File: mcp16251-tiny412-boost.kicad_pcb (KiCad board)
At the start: 2 copper layers, 33 x 22.9 mm, 33 parts, among them J1 THT_Castellated, J2 JST_PH_Header, J3 THT_Castellated, J4 THT_Castellated, J5 THT_Castellated, J6 THT_Castellated, Q1 Q_PMOS_GSD, Q2 NPN_3904, Q3 Q_PMOS_GSD, Q4 Q_PMOS_GSD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

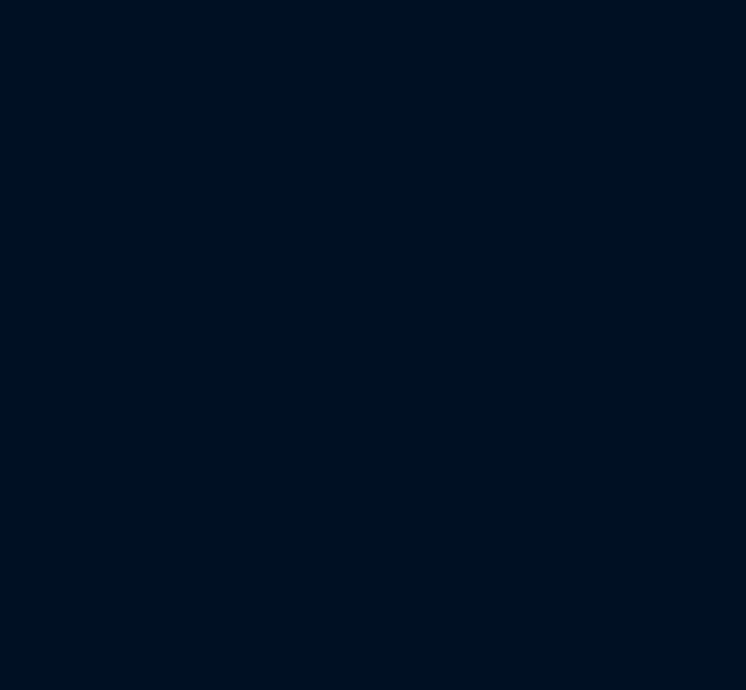
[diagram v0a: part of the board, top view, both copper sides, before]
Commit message: Add logic level shifter TXB104
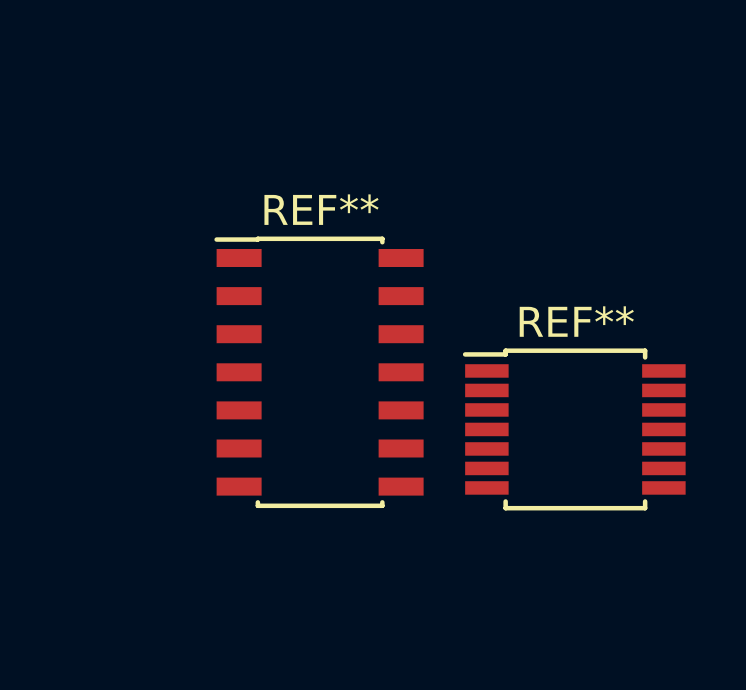
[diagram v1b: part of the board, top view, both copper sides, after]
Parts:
- added REF**: SOIC-14_3.9x8.7mm_Pitch1.27mm, Housings_SOIC:SOIC-14_3.9x8.7mm_Pitch1.27mm, F.Cu at (188.2, 89.3)
- added REF**: TSSOP-14_4.4x5mm_Pitch0.65mm, Housings_SSOP:TSSOP-14_4.4x5mm_Pitch0.65mm, F.Cu at (196.7, 91.2)
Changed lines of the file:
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@@
     (tracks 126)
     (zones 0)
-    (modules 33)
+    (modules 35)
     (nets 19)
   )
@@
       (net 13 uC_RESET))
   )
+  (module Housings_SOIC:SOIC-14_3.9x8.7mm_Pitch1.27mm (layer F.Cu)
+    (at 188.1505 89.281)
+    (descr "14-Lead Plastic Small Outline (SL) - Narrow, 3.90 mm Body [SOIC] (see Microchip Packaging Specification 00000049BS.pdf)")
+    (tags "SOIC 1.27")
+    (attr smd)
+    (fp_text reference REF** (at 0 -5.375) (layer F.SilkS)
+      (effects (font (size 1 1) (thickness 0.15)))
+    )
+    (fp_text value SOIC-14_3.9x8.7mm_Pitch1.27mm (at 0 5.375) (layer F.Fab)
+      (effects (font (size 1 1) (thickness 0.15)))
+    )
+    (fp_text user %R (at 0 0) (layer F.Fab)
+      (effects (font (size 0.9 0.9) (thickness 0.135)))
+    )
+    (fp_line (start -0.95 -4.35) (end 1.95 -4.35) (layer F.Fab) (width 0.15))
+    (fp_line (start 1.95 -4.35) (end 1.95 4.35) (layer F.Fab) (width 0.15))
+    (fp_line (start 1.95 4.35) (end -1.95 4.35) (layer F.Fab) (width 0.15))
+    (fp_line (start -1.95 4.35) (end -1.95 -3.35) (layer F.Fab) (width 0.15))
+    (fp_line (start -1.95 -3.35) (end -0.95 -4.35) (layer F.Fab) (width 0.15))
+    (fp_line (start -3.7 -4.65) (end -3.7 4.65) (layer F.CrtYd) (width 0.05))
+    (fp_line (start 3.7 -4.65) (end 3.7 4.65) (layer F.CrtYd) (width 0.05))
+    (fp_line (start -3.7 -4.65) (end 3.7 -4.65) (layer F.CrtYd) (width 0.05))
+    (fp_line (start -3.7 4.65) (end 3.7 4.65) (layer F.CrtYd) (width 0.05))
+    (fp_line (start -2.075 -4.45) (end -2.075 -4.425) (layer F.SilkS) (width 0.15))
+    (fp_line (start 2.075 -4.45) (end 2.075 -4.335) (layer F.SilkS) (width 0.15))
+    (fp_line (start 2.075 4.45) (end 2.075 4.335) (layer F.SilkS) (width 0.15))
+    (fp_line (start -2.075 4.45) (end -2.075 4.335) (layer F.SilkS) (width 0.15))
+    (fp_line (start -2.075 -4.45) (end 2.075 -4.45) (layer F.SilkS) (width 0.15))
+    (fp_line (start -2.075 4.45) (end 2.075 4.45) (layer F.SilkS) (width 0.15))
+    (fp_line (start -2.075 -4.425) (end -3.45 -4.425) (layer F.SilkS) (width 0.15))
+    (pad 1 smd rect (at -2.7 -3.81) (size 1.5 0.6) (layers F.Cu F.Paste F.Mask))
+    (pad 2 smd rect (at -2.7 -2.54) (size 1.5 0.6) (layers F.Cu F.Paste F.Mask))
+    (pad 3 smd rect (at -2.7 -1.27) (size 1.5 0.6) (layers F.Cu F.Paste F.Mask))
+    (pad 4 smd rect (at -2.7 0) (size 1.5 0.6) (layers F.Cu F.Paste F.Mask))
+    (pad 5 smd rect (at -2.7 1.27) (size 1.5 0.6) (layers F.Cu F.Paste F.Mask))
+    (pad 6 smd rect (at -2.7 2.54) (size 1.5 0.6) (layers F.Cu F.Paste F.Mask))
+    (pad 7 smd rect (at -2.7 3.81) (size 1.5 0.6) (layers F.Cu F.Paste F.Mask))
+    (pad 8 smd rect (at 2.7 3.81) (size 1.5 0.6) (layers F.Cu F.Paste F.Mask))
+    (pad 9 smd rect (at 2.7 2.54) (size 1.5 0.6) (layers F.Cu F.Paste F.Mask))
+    (pad 10 smd rect (at 2.7 1.27) (size 1.5 0.6) (layers F.Cu F.Paste F.Mask))
+    (pad 11 smd rect (at 2.7 0) (size 1.5 0.6) (layers F.Cu F.Paste F.Mask))
+    (pad 12 smd rect (at 2.7 -1.27) (size 1.5 0.6) (layers F.Cu F.Paste F.Mask))
+    (pad 13 smd rect (at 2.7 -2.54) (size 1.5 0.6) (layers F.Cu F.Paste F.Mask))
+    (pad 14 smd rect (at 2.7 -3.81) (size 1.5 0.6) (layers F.Cu F.Paste F.Mask))
+    (model ${KISYS3DMOD}/Housings_SOIC.3dshapes/SOIC-14_3.9x8.7mm_Pitch1.27mm.wrl
+      (at (xyz 0 0 0))
+      (scale (xyz 1 1 1))
+      (rotate (xyz 0 0 0))
+    )
+  )
+  (module Housings_SSOP:TSSOP-14_4.4x5mm_Pitch0.65mm (layer F.Cu)
+    (at 196.6595 91.186)
+    (descr "14-Lead Plastic Thin Shrink Small Outline (ST)-4.4 mm Body [TSSOP] (see Microchip Packaging Specification 00000049BS.pdf)")
+    (tags "SSOP 0.65")
+    (attr smd)
+    (fp_text reference REF** (at 0 -3.55) (layer F.SilkS)
+      (effects (font (size 1 1) (thickness 0.15)))
+    )
+    (fp_text value TSSOP-14_4.4x5mm_Pitch0.65mm (at 0 3.55) (layer F.Fab)
+      (effects (font (size 1 1) (thickness 0.15)))
+    )
+    (fp_line (start -1.2 -2.5) (end 2.2 -2.5) (layer F.Fab) (width 0.15))
+    (fp_line (start 2.2 -2.5) (end 2.2 2.5) (layer F.Fab) (width 0.15))
+    (fp_line (start 2.2 2.5) (end -2.2 2.5) (layer F.Fab) (width 0.15))
+    (fp_line (start -2.2 2.5) (end -2.2 -1.5) (layer F.Fab) (width 0.15))
+    (fp_line (start -2.2 -1.5) (end -1.2 -2.5) (layer F.Fab) (width 0.15))
+    (fp_line (start -3.95 -2.8) (end -3.95 2.8) (layer F.CrtYd) (width 0.05))
+    (fp_line (start 3.95 -2.8) (end 3.95 2.8) (layer F.CrtYd) (width 0.05))
+    (fp_line (start -3.95 -2.8) (end 3.95 -2.8) (layer F.CrtYd) (width 0.05))
+    (fp_line (start -3.95 2.8) (end 3.95 2.8) (layer F.CrtYd) (width 0.05))
+    (fp_line (start -2.325 -2.625) (end -2.325 -2.5) (layer F.SilkS) (width 0.15))
+    (fp_line (start 2.325 -2.625) (end 2.325 -2.4) (layer F.SilkS) (width 0.15))
+    (fp_line (start 2.325 2.625) (end 2.325 2.4) (layer F.SilkS) (width 0.15))
+    (fp_line (start -2.325 2.625) (end -2.325 2.4) (layer F.SilkS) (width 0.15))
+    (fp_line (start -2.325 -2.625) (end 2.325 -2.625) (layer F.SilkS) (width 0.15))
+    (fp_line (start -2.325 2.625) (end 2.325 2.625) (layer F.SilkS) (width 0.15))
+    (fp_line (start -2.325 -2.5) (end -3.675 -2.5) (layer F.SilkS) (width 0.15))
+    (fp_text user %R (at 0 0) (layer F.Fab)
+      (effects (font (size 0.8 0.8) (thickness 0.15)))
+    )
+    (pad 1 smd rect (at -2.95 -1.95) (size 1.45 0.45) (layers F.Cu F.Paste F.Mask))
+    (pad 2 smd rect (at -2.95 -1.3) (size 1.45 0.45) (layers F.Cu F.Paste F.Mask))
+    (pad 3 smd rect (at -2.95 -0.65) (size 1.45 0.45) (layers F.Cu F.Paste F.Mask))
+    (pad 4 smd rect (at -2.95 0) (size 1.45 0.45) (layers F.Cu F.Paste F.Mask))
+    (pad 5 smd rect (at -2.95 0.65) (size 1.45 0.45) (layers F.Cu F.Paste F.Mask))
+    (pad 6 smd rect (at -2.95 1.3) (size 1.45 0.45) (layers F.Cu F.Paste F.Mask))
+    (pad 7 smd rect (at -2.95 1.95) (size 1.45 0.45) (layers F.Cu F.Paste F.Mask))
+    (pad 8 smd rect (at 2.95 1.95) (size 1.45 0.45) (layers F.Cu F.Paste F.Mask))
+    (pad 9 smd rect (at 2.95 1.3) (size 1.45 0.45) (layers F.Cu F.Paste F.Mask))
+    (pad 10 smd rect (at 2.95 0.65) (size 1.45 0.45) (layers F.Cu F.Paste F.Mask))
+    (pad 11 smd rect (at 2.95 0) (size 1.45 0.45) (layers F.Cu F.Paste F.Mask))
+    (pad 12 smd rect (at 2.95 -0.65) (size 1.45 0.45) (layers F.Cu F.Paste F.Mask))
+    (pad 13 smd rect (at 2.95 -1.3) (size 1.45 0.45) (layers F.Cu F.Paste F.Mask))
+    (pad 14 smd rect (at 2.95 -1.95) (size 1.45 0.45) (layers F.Cu F.Paste F.Mask))
+    (model ${KISYS3DMOD}/Housings_SSOP.3dshapes/TSSOP-14_4.4x5mm_Pitch0.65mm.wrl
+      (at (xyz 0 0 0))
+      (scale (xyz 1 1 1))
+      (rotate (xyz 0 0 0))
+    )
+  )
   (gr_text B- (at 136.779 91.3892) (layer F.SilkS)

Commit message: Prepare for layout
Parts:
- removed C3: 100nF, MCP16251_module:R_0805_HS
- removed Q2: NPN_3904, MCP16251_module:SOT-23_HS
- removed Q3, Q4: Q_PMOS_GSD, MCP16251_module:SOT-23_HS
- removed R1, R4: 100k, MCP16251_module:R_0805_HS
- removed REF**: SOIC-14_3.9x8.7mm_Pitch1.27mm, Housings_SOIC:SOIC-14_3.9x8.7mm_Pitch1.27mm
- removed REF**: TSSOP-14_4.4x5mm_Pitch0.65mm, Housings_SSOP:TSSOP-14_4.4x5mm_Pitch0.65mm
- added C10: 0.1uF, MCP16251_module:0805_HS, F.Cu at (186.7, 67.3)
- added C11: 0.1uF, MCP16251_module:0805_HS, F.Cu at (199.4, 67.3)
- added C5: 0.1uF, MCP16251_module:0805_HS, F.Cu at (123.2, 80.0)
- added C6: 0.1uF, MCP16251_module:0805_HS, F.Cu at (130.8, 79.9)
- added C7: 0.1uF, MCP16251_module:0805_HS, F.Cu at (141.0, 78.7)
- added C8: 0.1uF, MCP16251_module:0805_HS, F.Cu at (152.4, 74.9)
- added J10: THT_Castellated, MCP16251_module:Conn_01x01_cast, F.Cu at (222.2, 66.0)
- added J11: THT_Castellated, MCP16251_module:Conn_01x01_cast, F.Cu at (222.2, 68.6)
- added J7: THT_Castellated, MCP16251_module:Conn_01x01_cast, F.Cu at (222.2, 88.9)
- added J8: THT_Castellated, MCP16251_module:Conn_01x01_cast, F.Cu at (222.2, 91.4)
- added J9: THT_Castellated, MCP16251_module:Conn_01x01_cast, F.Cu at (222.2, 94.0)
- added R9: 100k, MCP16251_module:0805_HS, F.Cu at (199.4, 76.2)
- added U5: TXB0104, MCP16251_module:SOIC-14_3.9x8.7mm_Pitch1.27mm_HS, F.Cu at (193.0, 72.4)
- C1, C2, C4, F1: footprint MCP16251_module:R_1206_HS -> MCP16251_module:1206_HS
- J1: value THT_Castellated -> JST_PH_Header; footprint MCP16251_module:Conn_01x02_cast -> Connectors_JST:JST_PH_S2B-PH-K_02x2.00mm_Angled
- J2: value JST_PH_Header -> THT_Castellated; footprint Connectors_JST:JST_PH_S2B-PH-K_02x2.00mm_Angled -> MCP16251_module:Conn_01x01_cast
- J3: footprint MCP16251_module:Conn_01x02_cast_mirrored -> MCP16251_module:Conn_01x01_cast
- JP1, JP2, R2, R3, R5: footprint MCP16251_module:R_0805_HS -> MCP16251_module:0805_HS
- R6: value 100k -> R; footprint MCP16251_module:R_0805_HS -> MCP16251_module:0805_HS
- R7: value 1k -> R; footprint MCP16251_module:R_0805_HS -> MCP16251_module:0805_HS
- R8: value 100k -> 3.3k; footprint MCP16251_module:R_0805_HS -> MCP16251_module:0805_HS
- SW2: footprint Buttons_Switches_SMD:SW_SPST_TL3342 -> MCP16251_module:SW_SPST_PUSH_6mm_3mm
- U3: value MIC803 -> attiny412; footprint MCP16251_module:SOT-23_HS -> MCP16251_module:SOIC-8_3.9x4.9mm_Pitch1.27_HSmm
- U4: value MIC2777 -> AP7354
- moved J4 80.8 mm to (222.2, 76.2), turned to 180 degrees
- moved J5 76.7 mm to (222.2, 82.5), turned to 180 degrees
- moved J6 73.7 mm to (222.2, 85.1), turned to 180 degrees
- moved JP2 65.5 mm to (215.9, 71.1)
- moved U2 59.4 mm to (210.8, 78.7)
- moved U4 46.3 mm to (127.0, 80.0), turned to 0 degrees
- moved J3 40.4 mm to (128.3, 71.1), turned to 0 degrees
- moved J1 26.7 mm to (130.8, 62.2), turned to 270 degrees
- moved R8 23.7 mm to (152.4, 80.0)
- moved R5 21.4 mm to (161.3, 101.6), turned to 0 degrees
- moved R3 20.6 mm to (172.7, 92.7), turned to 0 degrees
- moved R7 20.1 mm to (157.5, 74.9), turned to 90 degrees
- moved JP1 19.1 mm to (141.0, 61.0), turned to 0 degrees
- moved SW1 17.8 mm to (142.2, 63.5), turned to 90 degrees
- moved C2 17.6 mm to (174.0, 97.8)
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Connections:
- J4 pad 1: PWR_CONTROL -> VIN_HV
- J5 pad 1: uC_ADC -> UPDI_HV
- J6 pad 1: uC_RESET -> GND
- JP1 pad 2: Vbat_raw_sense -> Net-(JP1-Pad2)
- JP2 pad 1: Net-(JP2-Pad1) -> VIN_HV
- JP2 pad 2: GND -> 5V
- Q1 pad 1: Net-(JP2-Pad1) -> GND
- Q1 pad 2: Vbat_raw_sense -> VBAT
- Q1 pad 3: VBAT -> Net-(JP1-Pad2)
- R5 pad 1: PWR_CONTROL -> BOOST_EN
- R6 pad 1: BOOST_EN -> VBAT
- R6 pad 2: GND -> Net-(C8-Pad2)
- R7 pad 1: uC_ADC -> Net-(C8-Pad2)
- R7 pad 2: Net-(Q4-Pad3) -> GND
- R8 pad 1: Net-(Q3-Pad1) -> UPDI
- R8 pad 2: Net-(Q3-Pad2) -> Net-(R8-Pad2)
- SW1 pad 1: Vbat_raw_sense -> Net-(JP1-Pad2)
- SW2 pad 1: GND -> Net-(R8-Pad2)
- SW2 pad 2: Net-(JP2-Pad1) -> GND
- U2 pad 2: BOOST_EN -> SHIFT_EN
- U2 pad 3: VBAT -> VIN_HV
- U3 pad 1: GND -> 2V5
- U3 pad 2: uC_RESET -> Net-(C8-Pad2)
- U3 pad 3: 5V -> BOOST_EN
- U4 pad 1: (no net) -> VBAT
- U4 pad 3: Net-(Q3-Pad1) -> VBAT
- U4 pad 5: 5V -> 2V5
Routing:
- net GND: track 30.3 -> 0.00 mm, vias 9 -> 0
- net Vbat_raw_sense: track 27.8 -> 0.00 mm, vias 2 -> 0
- net Net-(JP2-Pad1): track 23.7 -> 0.00 mm
- net VBAT: track 21.3 -> 0.00 mm, vias 2 -> 0
- net 5V: track 17.8 -> 0.00 mm
- net VBAT_RAW: track 9.84 -> 0.00 mm
- net Net-(R5-Pad1): track 9.79 -> 0.00 mm
- net Net-(R2-Pad2): track 7.54 -> 0.00 mm
- net Net-(L1-Pad2): track 6.14 -> 0.00 mm
- net Net-(Q2-Pad1): track 2.17 -> 0.00 mm
- removed copper zone on B.Cu, net GND
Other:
- board outline removed
- board text removed: "0R"
- board text removed: "Adj; FB=1.23V"
- board text removed: "B+"
- board text removed: "B-"
- board text removed: "B- GND"
- board text removed: "BAT"
- board text removed: "BAT sense"
- board text removed: "FB"
- board text removed: "GND"
- board text removed: "GND B-"
- board text removed: "MCP16251T boost module rev. 1 (c) Vlad Belous; CC BY-SA"
- board text removed: "OFF"
- board text removed: "ON"
- board text removed: "PWR"
- board text removed: "PWR control"
- board text removed: "R-HI"
- board text removed: "R-LO"
- board text removed: "VOUT"
- board text removed: "Vout"
- board text removed: "ctrl"
- board text removed: "sense"

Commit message: Approx boost circuit arrangement
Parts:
- moved RV1 9.44 mm to (172.8, 99.2), turned to 0 degrees
- moved R3 8.96 mm to (170.0, 101.2), turned to 270 degrees
- moved C2 8.87 mm to (168.0, 91.2)
- moved C1 6.24 mm to (168.0, 93.5)
- moved R5 5.21 mm to (166.5, 101.5)
- moved R2 5.12 mm to (170.0, 97.2), turned to 270 degrees
- moved C4 3.30 mm to (162.8, 96.0), turned to 270 degrees
- moved L1 2.34 mm to (158.5, 97.0), turned to 270 degrees
- moved U1 0.31 mm to (166.2, 97.5), turned to 90 degrees

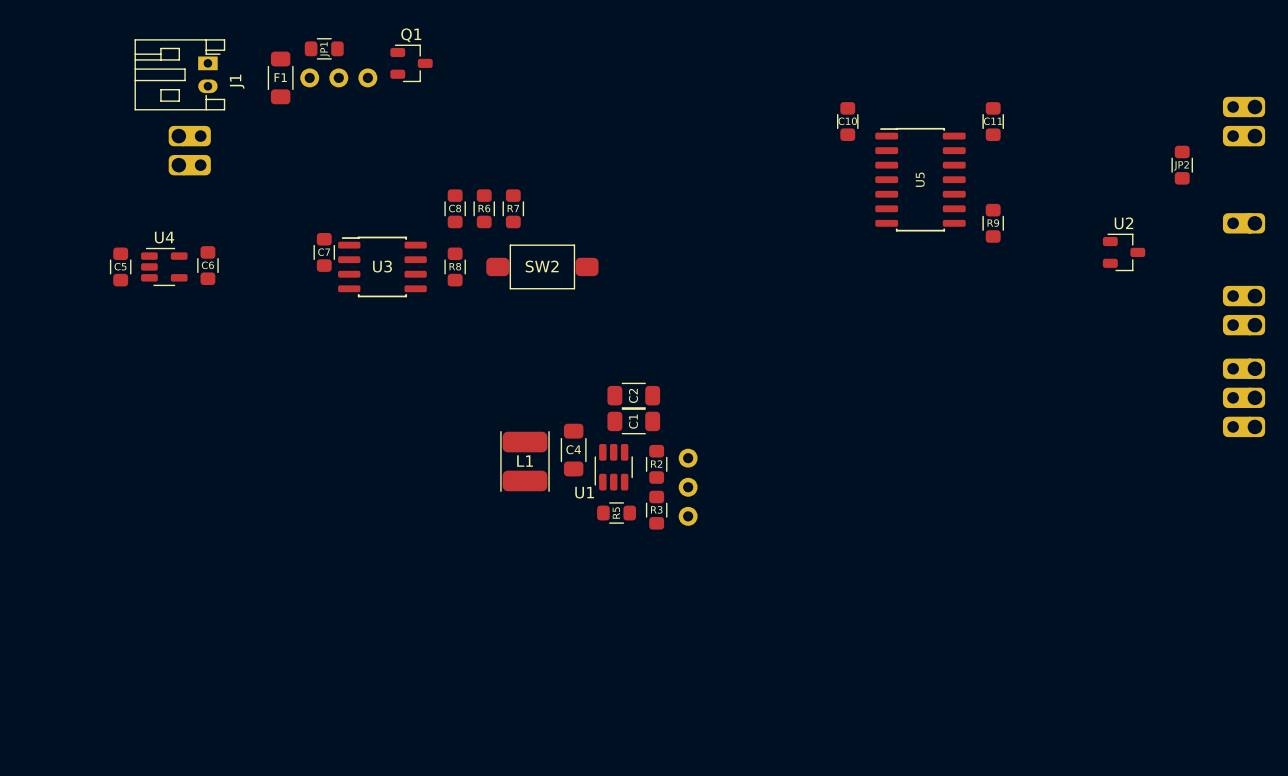
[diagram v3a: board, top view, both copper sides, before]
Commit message: Complete layout candidate, no routing
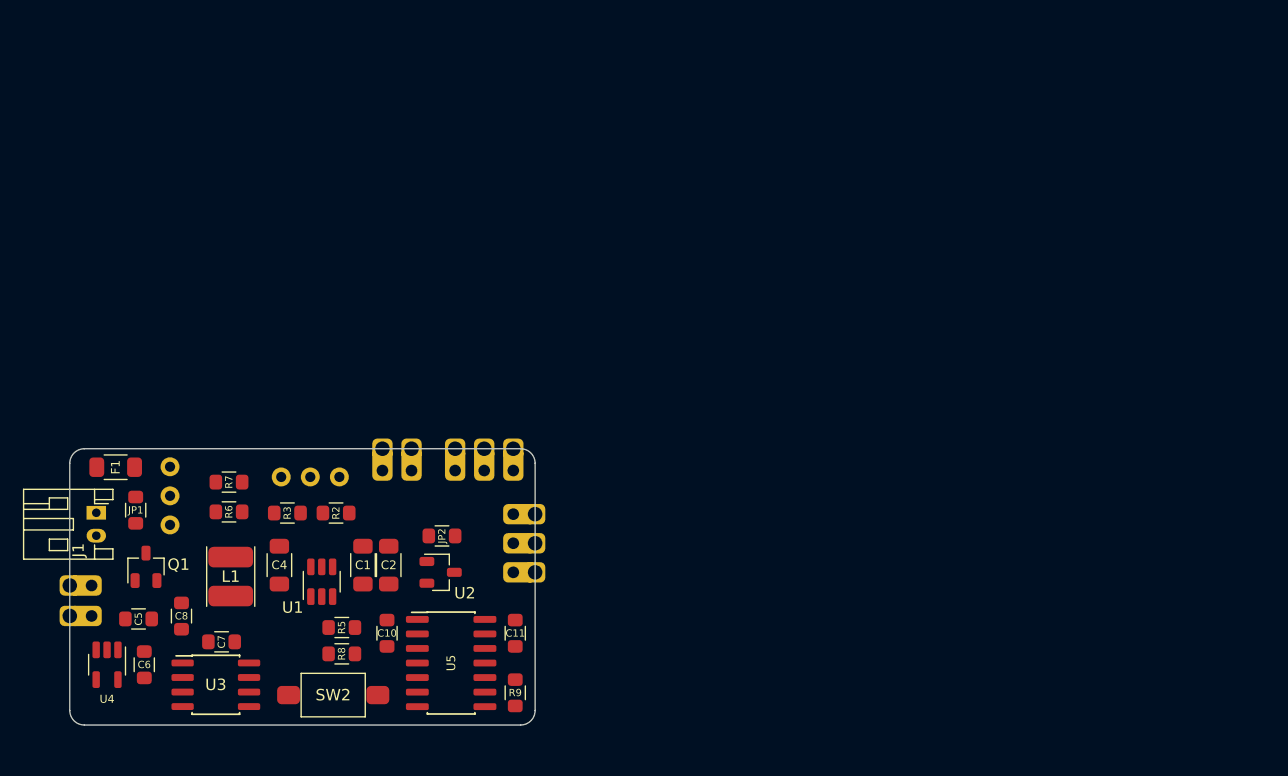
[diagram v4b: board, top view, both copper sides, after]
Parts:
- moved J10 81.8 mm to (146.1, 95.9), turned to 270 degrees
- moved J11 78.6 mm to (148.6, 95.9), turned to 270 degrees
- moved J4 72.6 mm to (152.4, 95.9), turned to 270 degrees
- moved JP2 72.3 mm to (151.2, 103.5), turned to 180 degrees
- moved J5 68.6 mm to (154.9, 95.9), turned to 270 degrees
- moved U2 65.9 mm to (151.1, 106.7)
- moved J6 65.7 mm to (157.5, 95.9), turned to 270 degrees
- moved J7 64.1 mm to (159.4, 101.6)
- moved J8 64.1 mm to (159.4, 104.1)
- moved J9 64.1 mm to (159.4, 106.7)
- moved C11 61.2 mm to (157.7, 112.0)
- moved C10 60.1 mm to (146.4, 112.0)
- moved U5 58.8 mm to (152.1, 114.6)
- moved R9 58.5 mm to (157.7, 117.2)
- moved Q1 49.7 mm to (125.4, 106.2), turned to 90 degrees
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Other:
- board outline added: 40.6 x 24.1 mm
